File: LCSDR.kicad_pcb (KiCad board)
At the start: 2 copper layers, 150 x 95 mm, 75 parts, among them J1 MIC_PTT, J10 Conn_01x01, J11 Conn_01x01, J13 Jack-DC, J2 Conn_01x30, J3 Audio-Jack-3_2Switches, J4 Conn_01x30, J5 USB_B_Mini, J6 IDC10 Serial Wire, J8 Conn_01x01, J9 Conn_01x01, U1 SI5351A, U16 WM8731_alt, U2 FM24CL16B, U3 STM32F401RCTx, U5 MC34063, U7 78M09, Y1 20Mhz, Y2 Crystal

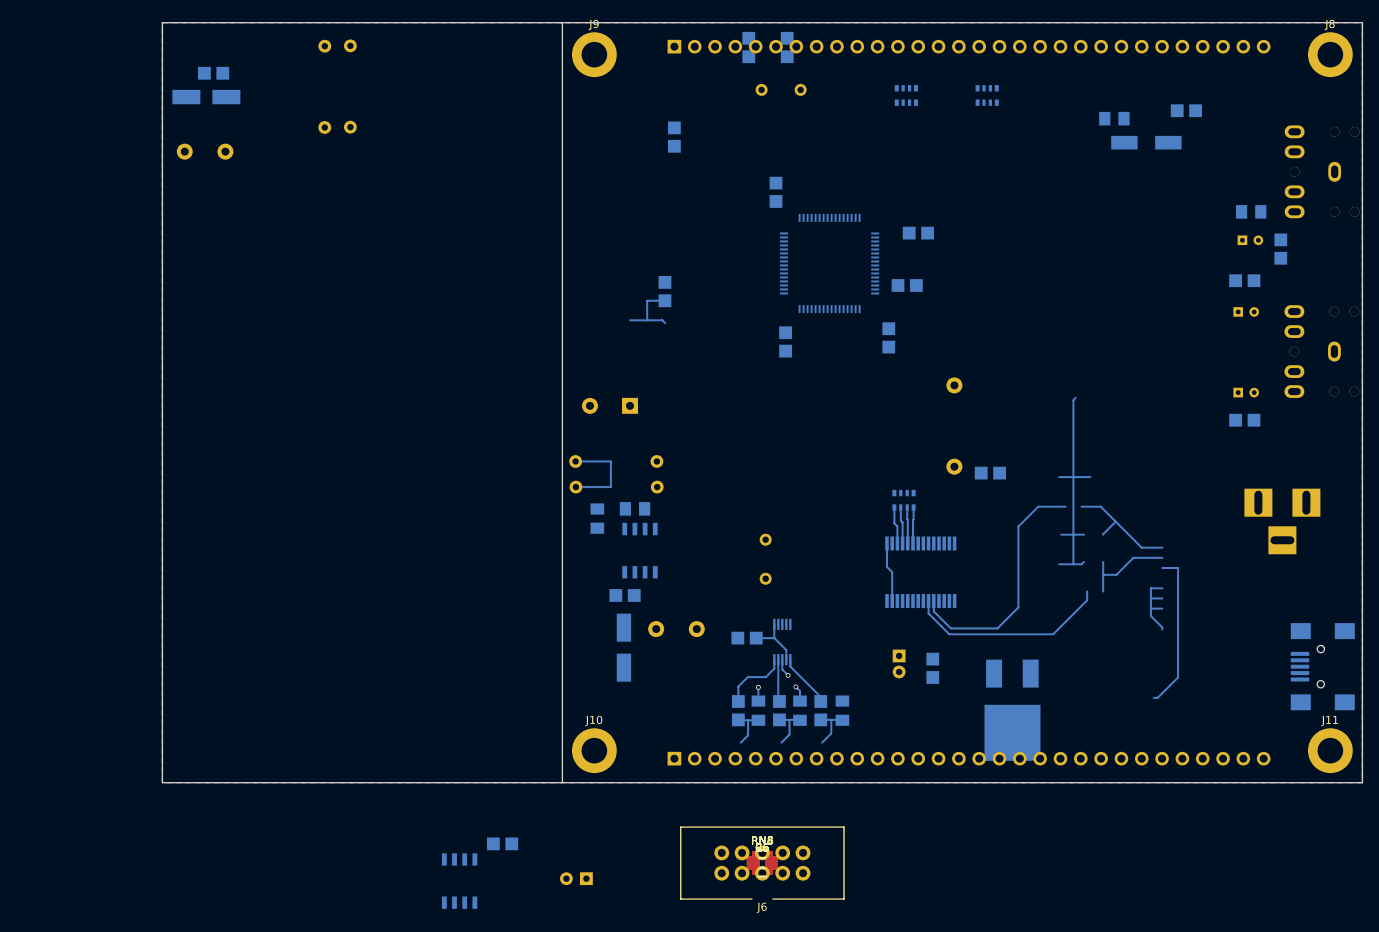
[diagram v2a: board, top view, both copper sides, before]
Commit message: PCB almost ready, needs some GND vias
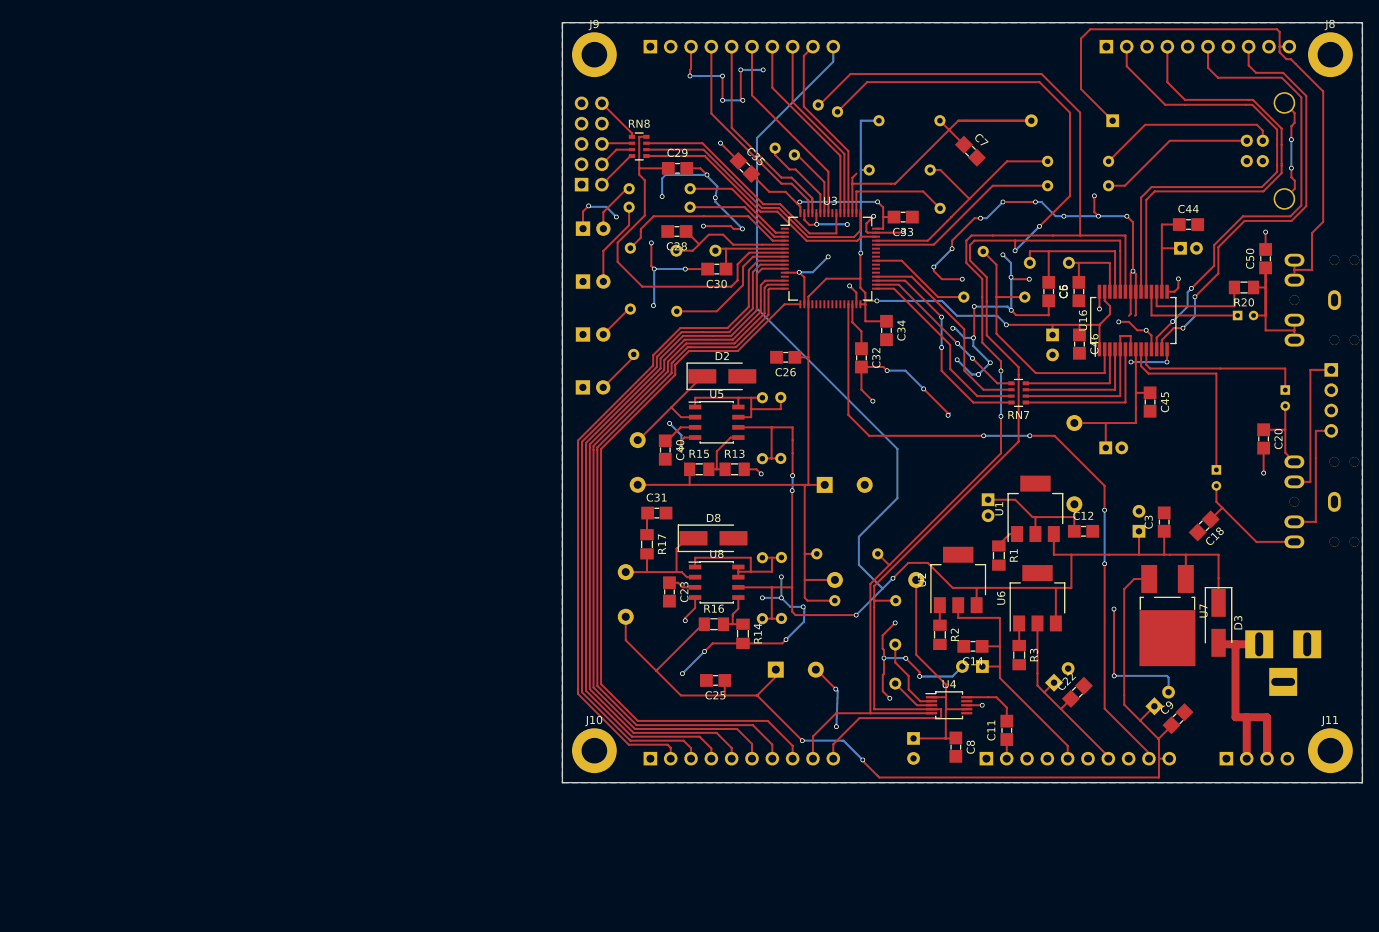
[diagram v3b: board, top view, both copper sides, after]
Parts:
- removed C2: 100nF, UI:C_1206_0603
- removed C36: 10uF, Capacitors_THT:CP_Radial_D6.3mm_P2.50mm
- removed C41: 180pF, UI:C_1206_0603
- removed RN2, RN3, RN4, RN5, RN6: 47, Resistors_SMD:R_Array_Convex_4x0603
- removed Y2: Crystal, Crystals:Crystal_HC49-U_Vertical
- added C10: 100uF, Capacitors_THT:CP_Radial_D6.3mm_P2.50mm, B.Cu at (167.5, 120.5)
- added C11: 100nF, UI:C_1206_0603, F.Cu at (170.6, 128.5)
- added C12: 100nF, UI:C_1206_0603, F.Cu at (180.1, 103.6)
- added C13: 100uF, Capacitors_THT:CP_Radial_D6.3mm_P2.50mm, B.Cu at (189.0, 125.5)
- added C14: 100nF, UI:C_1206_0603, F.Cu at (166.3, 118.0)
- added C15: 100uF, Capacitors_THT:CP_Radial_D6.3mm_P2.50mm, B.Cu at (158.9, 129.5)
- added C16: 100uF, Capacitors_THT:CP_Radial_D6.3mm_P2.50mm, B.Cu at (176.4, 122.5)
- added C21: 100uF, Capacitors_THT:CP_Radial_D6.3mm_P2.50mm, B.Cu at (187.1, 103.6)
- added C22: 100nF, UI:C_1206_0603, F.Cu at (179.4, 123.7)
- added C23: 180pF, UI:C_1206_0603, F.Cu at (128.4, 111.2)
- added C24: 1000uF, Capacitors_THT:CP_Radial_D10.0mm_P5.00mm, B.Cu at (141.7, 120.9)
- added C25: 100nF, UI:C_1206_0603, F.Cu at (134.2, 122.2)
- added C31: 100nF, UI:C_1206_0603, F.Cu at (126.8, 101.3)
- added C8: 100nF, UI:C_1206_0603, F.Cu at (164.2, 130.6)
- added C9: 100nF, UI:C_1206_0603, F.Cu at (191.9, 127.0)
- added D4: LED, LEDs:LED_D5.0mm_FlatTop, B.Cu at (117.6, 65.8)
- added D5: LED, LEDs:LED_D5.0mm_FlatTop, B.Cu at (117.6, 72.4)
- added D6: LED, LEDs:LED_D5.0mm_FlatTop, B.Cu at (117.6, 79.0)
- added D7: LED, LEDs:LED_D5.0mm_FlatTop, B.Cu at (117.6, 85.6)
- added D8: SS14, Diodes_SMD:D_SMA_Handsoldering, F.Cu at (133.9, 104.5)
- added J12: Conn_01x10, Pin_Headers:Pin_Header_Straight_1x10_Pitch2.54mm, B.Cu at (126.0, 43.0)
- added J14: Conn_01x04, Pin_Headers:Pin_Header_Straight_1x04_Pitch2.54mm, B.Cu at (198.0, 132.0)
- added J15: SPEAKER, Pin_Headers:Pin_Header_Straight_1x04_Pitch2.54mm, B.Cu at (211.1, 83.4)
- added J7: Conn_01x10, Pin_Headers:Pin_Header_Straight_1x10_Pitch2.54mm, B.Cu at (126.0, 132.0)
- added L1: 100uH, Choke_Axial_ThroughHole:Choke_Horizontal_RM10mm, B.Cu at (154.1, 109.7)
- added R14: 11k, UI:R_1206_0603, F.Cu at (137.6, 116.4)
- added R16: 18k, UI:R_1206_0603, F.Cu at (133.9, 115.2)
- added R17: 18k, UI:R_1206_0603, F.Cu at (125.6, 105.2)
- added R18: 4.7k, Resistors_THT:R_Axial_DIN0204_L3.6mm_D1.6mm_P7.62mm_Horizontal, B.Cu at (123.3, 60.8)
- added R19: 4.7k, Resistors_THT:R_Axial_DIN0204_L3.6mm_D1.6mm_P7.62mm_Horizontal, B.Cu at (123.3, 63.1)
- added R21: 4.7k, Resistors_THT:R_Axial_DIN0204_L3.6mm_D1.6mm_P7.62mm_Horizontal, B.Cu at (123.5, 75.8)
- added R22: 4.7k, Resistors_THT:R_Axial_DIN0204_L3.6mm_D1.6mm_P7.62mm_Horizontal, B.Cu at (123.9, 81.5)
- added R23: 47R, Resistors_THT:R_Axial_DIN0204_L3.6mm_D1.6mm_P7.62mm_Horizontal, B.Cu at (141.6, 55.7)
- added R24: 47R, Resistors_THT:R_Axial_DIN0204_L3.6mm_D1.6mm_P7.62mm_Horizontal, B.Cu at (183.3, 57.3)
- added R25: 47R, Resistors_THT:R_Axial_DIN0204_L3.6mm_D1.6mm_P7.62mm_Horizontal, B.Cu at (183.3, 60.4)
- added R26: 4.7k, Resistors_THT:R_Axial_DIN0204_L3.6mm_D1.6mm_P7.62mm_Horizontal, B.Cu at (153.3, 58.4)
- added R27: 47R, Resistors_THT:R_Axial_DIN0204_L3.6mm_D1.6mm_P7.62mm_Horizontal, B.Cu at (144.0, 56.5)
- added R7: 56, Resistors_THT:R_Axial_DIN0204_L3.6mm_D1.6mm_P7.62mm_Horizontal, B.Cu at (172.8, 74.3)
- added R8: 56, Resistors_THT:R_Axial_DIN0204_L3.6mm_D1.6mm_P7.62mm_Horizontal, B.Cu at (167.6, 68.6)
- added U4: SI5351A, Housings_SSOP:MSOP-10_3x3mm_Pitch0.5mm, F.Cu at (163.3, 125.3)
- added U6: LD1117S33TR, TO_SOT_Packages_SMD:SOT-223, F.Cu at (174.4, 111.9)
- added U8: MC34063, UI:SOIC-8_3.9x4.9mm_Pitch1.27mm, F.Cu at (134.3, 110.0)
- added Y3: 12.288Mhz, Crystals:Crystal_HC49-U_Vertical, B.Cu at (178.3, 70.0)
- added Y4: Crystal, Crystals:Crystal_HC49-U_Vertical, B.Cu at (156.6, 122.6)
- C1, C4: value 100nF -> 10uF; footprint UI:C_1206_0603 -> Capacitors_THT:CP_Radial_D5.0mm_P2.00mm
- C116: footprint Capacitors_ThroughHole:CP_Radial_D5.0mm_P2.00mm -> Capacitors_THT:CP_Radial_D5.0mm_P2.00mm
- C18, C20, C26, C28, C29, C3, C30, C32, C33, C34, C35, C40, C44, C45, C46, C50, C7, D2, D3, R13, R15, R20, RN7, U16, U3, U5, U7: moved to F.Cu
- C27: value 100nF -> 100uF; footprint UI:C_1206_0603 -> Capacitors_THT:CP_Radial_D6.3mm_P2.50mm
- C38: footprint Capacitors_ThroughHole:CP_Radial_D10.0mm_P5.00mm -> Capacitors_THT:CP_Radial_D10.0mm_P5.00mm
- D1: footprint Diodes_SMD:D_MiniMELF_Handsoldering -> Diodes_THT:D_DO-35_SOD27_P10.16mm_Horizontal
- J2, J4: value Conn_01x30 -> Conn_01x10; footprint Pin_Headers:Pin_Header_Straight_1x30_Pitch2.54mm -> Pin_Headers:Pin_Header_Straight_1x10_Pitch2.54mm
- J5: value USB_B_Mini -> USB_B; footprint Connectors:USB_Mini-B -> Connectors:USB_B
- J6: value IDC10 Serial Wire -> SWO; footprint UI:USBBLASTER -> Pin_Headers:Pin_Header_Straight_2x05_Pitch2.54mm; moved to B.Cu
- L2, L3: footprint Choke_Toroid_ThroughHole:Choke_Toroid_5x10mm_Vertical -> Choke_Toroid_ThroughHole:Choke_Toroid_6,5x13mm_Vertical
- R1, R2, R3: value 100 -> 10; moved to F.Cu
- R10, R11, R12, R9: footprint Resistors_ThroughHole:R_Axial_DIN0207_L6.3mm_D2.5mm_P10.16mm_Horizontal -> Resistors_THT:R_Axial_DIN0204_L3.6mm_D1.6mm_P7.62mm_Horizontal
- R4: footprint UI:R_1206_0603 -> Resistors_THT:R_Axial_DIN0204_L3.6mm_D1.6mm_P7.62mm_Horizontal
- R5, R6: footprint UI:R_1206_0603 -> Resistors_THT:R_Axial_DIN0204_L3.6mm_D1.6mm_P7.62mm_Horizontal; moved to B.Cu
- U1: value SI5351A -> LD1117S33TR; footprint Housings_SSOP:MSOP-10_3x3mm_Pitch0.5mm -> TO_SOT_Packages_SMD:SOT-223; moved to F.Cu
- U2: value FM24CL16B -> LD1117S33TR; footprint Housings_SOIC:SOIC-8_3.9x4.9mm_Pitch1.27mm -> TO_SOT_Packages_SMD:SOT-223; moved to F.Cu
- moved D3 142.6 mm to (197.0, 115.0), turned to 270 degrees
- moved J2 104.1 mm to (183.0, 43.0)
- moved J4 97.2 mm to (168.0, 132.0)
- moved C27 93.7 mm to (176.3, 79.0), turned to 270 degrees
- moved RN8 90.9 mm to (124.6, 55.5)
- moved R10 88.2 mm to (140.0, 114.5), turned to 90 degrees
- moved J6 87.8 mm to (117.4, 60.2)
- moved C5 81.7 mm to (179.6, 73.6), turned to 90 degrees
- moved C6 79.9 mm to (175.8, 73.6), turned to 270 degrees
- moved R12 78.4 mm to (142.4, 106.8), turned to 270 degrees
- moved U2 72.8 mm to (164.5, 109.7)
- moved L3 67.5 mm to (116.3, 108.2), turned to 0 degrees
- moved C44 64.0 mm to (193.3, 65.2), turned to 0 degrees
- moved J5 63.9 mm to (200.6, 57.3), turned to 0 degrees
- moved C116 61.9 mm to (192.3, 68.2), turned to 0 degrees
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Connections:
- net MIC_BIAS renamed Net-(R20-Pad2)
- net MIC_IN renamed Net-(C49-Pad1)
- C1 pad 1: +3V3 -> Net-(C1-Pad1)
- C3 pad 1: CLK1 -> +12V
- C3 pad 2: Net-(C3-Pad2) -> GND
- C4 pad 1: CLK0 -> ANALOG_PS_AC
- C4 pad 2: Net-(C4-Pad2) -> GND
- C45 pad 1: GND -> Net-(C1-Pad1)
- C45 pad 2: Net-(C45-Pad2) -> GND
- D1 pad 1: Net-(D1-Pad1) -> PTT
- D3 pad 1: Net-(D3-Pad1) -> +12V
- D3 pad 2: GND -> +12VA
- J1 pad 2: Net-(D1-Pad1) -> PTT
- J1 pad 5: Net-(D1-Pad1) -> PTT
- J13 pad 1: +12V -> +12VA
- J2 pad 10: Net-(J2-Pad10) -> PTT
- J2 pad 2: CLK2 -> LINE_IN_LEFT
- J2 pad 4: CLK1 -> LINE_IN_RIGHT
- J2 pad 6: CLK0 -> LINE_OUT_LEFT
- J2 pad 7: Net-(J2-Pad7) -> GND
- J2 pad 8: Net-(J2-Pad8) -> LINE_OUT_RIGHT
- J2 pad 9: Net-(J2-Pad9) -> GND
- J3 pad 1: Net-(C19-Pad2) -> Net-(C17-Pad2)
- J3 pad 2: Net-(C17-Pad2) -> Net-(C19-Pad2)
- J4 pad 1: Net-(J4-Pad1) -> GND
- J4 pad 10: GND -> +9V
- J4 pad 2: Net-(J4-Pad2) -> CLK
- J4 pad 3: Net-(J4-Pad3) -> GND
- J4 pad 4: Net-(J4-Pad4) -> GND
- J4 pad 5: Net-(J4-Pad5) -> ROTATOR
- J4 pad 6: Net-(J4-Pad6) -> GND
- J4 pad 7: Net-(J4-Pad7) -> MIXER
- J4 pad 8: Net-(J4-Pad8) -> GND
- J4 pad 9: ADC -> IF_RX_TX
- J5 pad 1: Net-(J5-Pad1) -> (no net)
- J5 pad 4: Net-(J5-Pad4) -> GND
- J6 pad 1: MCU_VOLTAGE_33V -> (no net)
- J6 pad 7: Net-(J6-Pad7) -> (no net)
- J6 pad 8: Net-(J6-Pad8) -> (no net)
- L3 pad 1: Net-(D3-Pad1) -> Net-(D8-Pad1)
- L4 pad 1: Net-(C45-Pad2) -> ANALOG_PS_AC
- L4 pad 2: +3V3 -> Net-(C1-Pad1)
- R1 pad 1: CLK2 -> Net-(R1-Pad1)
- R12 pad 2: Net-(R12-Pad2) -> +12V
- R2 pad 1: CLK1 -> Net-(R2-Pad1)
- R3 pad 1: CLK0 -> Net-(R3-Pad1)
- RN8 pad 1: Net-(J6-Pad2) -> Net-(J6-Pad10)
- RN8 pad 2: Net-(J6-Pad4) -> Net-(J6-Pad6)
- RN8 pad 3: Net-(J6-Pad6) -> Net-(J6-Pad4)
- RN8 pad 4: Net-(J6-Pad10) -> Net-(J6-Pad2)
- RN8 pad 5: MCU_RESET -> SWDIO
- RN8 pad 6: SWO -> SWCLK
- RN8 pad 7: SWCLK -> SWO
- RN8 pad 8: SWDIO -> MCU_RESET
- U1 pad 1: +3V3 -> Net-(R1-Pad1)
- U1 pad 2: Net-(U1-Pad2) -> ANALOG_PS_AC
- U1 pad 3: Net-(U1-Pad3) -> +12V
- U1 pad 4: I2C_SCL -> (no net)
- U16 pad 14: Net-(C45-Pad2) -> Net-(C1-Pad1)
- U16 pad 8: Net-(C45-Pad2) -> Net-(C1-Pad1)
- U2 pad 1: Net-(U2-Pad1) -> Net-(R2-Pad1)
- U2 pad 2: Net-(U2-Pad2) -> ROTATOR
- U2 pad 3: Net-(U2-Pad3) -> +12V
- U2 pad 4: GND -> (no net)
- U3 pad 1: Net-(U3-Pad1) -> (no net)
- U3 pad 10: BAND2 -> IO4
- U3 pad 11: BAND3 -> IO5
- U3 pad 13: Net-(U3-Pad13) -> (no net)
- U3 pad 14: ATT -> IO6
- U3 pad 15: PREAMP -> IO7
- U3 pad 16: Net-(U3-Pad16) -> IO8
- U3 pad 17: Net-(U3-Pad17) -> IO9
- U3 pad 2: KEY_B -> LED3
- U3 pad 20: Net-(U3-Pad20) -> (no net)
- U3 pad 21: TX1 -> (no net)
- U3 pad 22: ENCODER_A -> (no net)
- U3 pad 23: ENCODER_B -> (no net)
- U3 pad 24: ADC -> (no net)
- U3 pad 25: Net-(U3-Pad25) -> (no net)
- U3 pad 26: Net-(U3-Pad26) -> (no net)
- U3 pad 27: Net-(U3-Pad27) -> (no net)
- U3 pad 28: Net-(U3-Pad28) -> (no net)
- U3 pad 29: Net-(U3-Pad29) -> IF_RX_TX
- U3 pad 3: KEY_C -> LED2
- U3 pad 37: I2S_MCLK -> (no net)
- U3 pad 38: Net-(U3-Pad38) -> (no net)
- U3 pad 39: TX2 -> (no net)
- U3 pad 4: KEY_D -> LED1
- U3 pad 40: I2C_SDA_MCU -> I2S_CLKIN_MCU
- U3 pad 41: I2C_SCL_MCU -> (no net)
- U3 pad 42: Net-(U3-Pad42) -> (no net)
- U3 pad 43: Net-(U3-Pad43) -> (no net)
- U3 pad 50: LCD_CE -> I2S_CLKIN_TEST_MCU
- U3 pad 51: LCD_CLK -> PTT_IN
- U3 pad 52: LCD_DC -> S2_RX_TX
- U3 pad 53: LCD_DIN -> S1_RX_TX
- U3 pad 54: Net-(U3-Pad54) -> IO3
- U3 pad 56: LCD_LIGHT -> (no net)
- U3 pad 57: I_IN_M2 -> IO2
- U3 pad 58: Q_IN_M1 -> I2C_SCL_MCU
- U3 pad 59: Q_IN_M2 -> I2C_SDA_MCU
- U3 pad 61: Net-(U3-Pad61) -> IO1
- U3 pad 62: Net-(U3-Pad62) -> IO0
- U3 pad 8: IO0 -> LED0
- U3 pad 9: BAND1 -> BAND
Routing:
- net GND: track 5.97 -> 329.4 mm, vias 3 -> 79
- net +12V: track 12.0 -> 219.4 mm, vias 0 -> 4
- net I2C_SCL: track 0.00 -> 175.8 mm, vias 0 -> 2
- net I2C_SDA: track 0.00 -> 167.5 mm, vias 0 -> 2
- net +3V3: track 24.0 -> 179.0 mm, vias 0 -> 5
- net +9V: track 0.00 -> 128.3 mm, vias 0 -> 2
- net IO9: track 0.00 -> 91.3 mm
- net IO8: track 0.00 -> 90.7 mm
- net IO7: track 0.00 -> 89.6 mm
- net IO5: track 0.00 -> 88.3 mm
- net IO6: track 0.00 -> 88.2 mm
- net (no net): track 87.2 -> 0.00 mm
- net IO4: track 0.00 -> 87.1 mm
- net BAND: track 0.00 -> 86.0 mm
- net IF_RX_TX: track 0.00 -> 86.0 mm, vias 0 -> 4
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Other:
- board size 150 x 95 mm -> 100 x 95 mm

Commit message: edit
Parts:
- moved R21 1.12 mm to (124.6, 76.0)
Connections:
- J7 pad 3: IO4 -> GND
- J7 pad 4: IO5 -> (no net)
- J7 pad 5: IO6 -> GND
- U3 pad 10: IO4 -> (no net)
- U3 pad 11: IO5 -> (no net)
- U3 pad 14: IO6 -> BAND
- U3 pad 9: BAND -> (no net)
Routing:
- net GND: track 329.4 -> 484.2 mm, vias 79 -> 113
- net IO5: track 88.3 -> 0.00 mm
- net IO6: track 88.2 -> 0.00 mm
- net IO4: track 87.1 -> 0.00 mm
- net BAND: track 86.0 -> 80.6 mm
- net Net-(D6-Pad2): track 4.71 -> 6.62 mm
- net MCU_RESET: track 47.0 -> 46.4 mm
- net LED1: track 22.9 -> 22.4 mm

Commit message: production
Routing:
- net GND: track 484.2 -> 898.3 mm, vias 113 -> 202

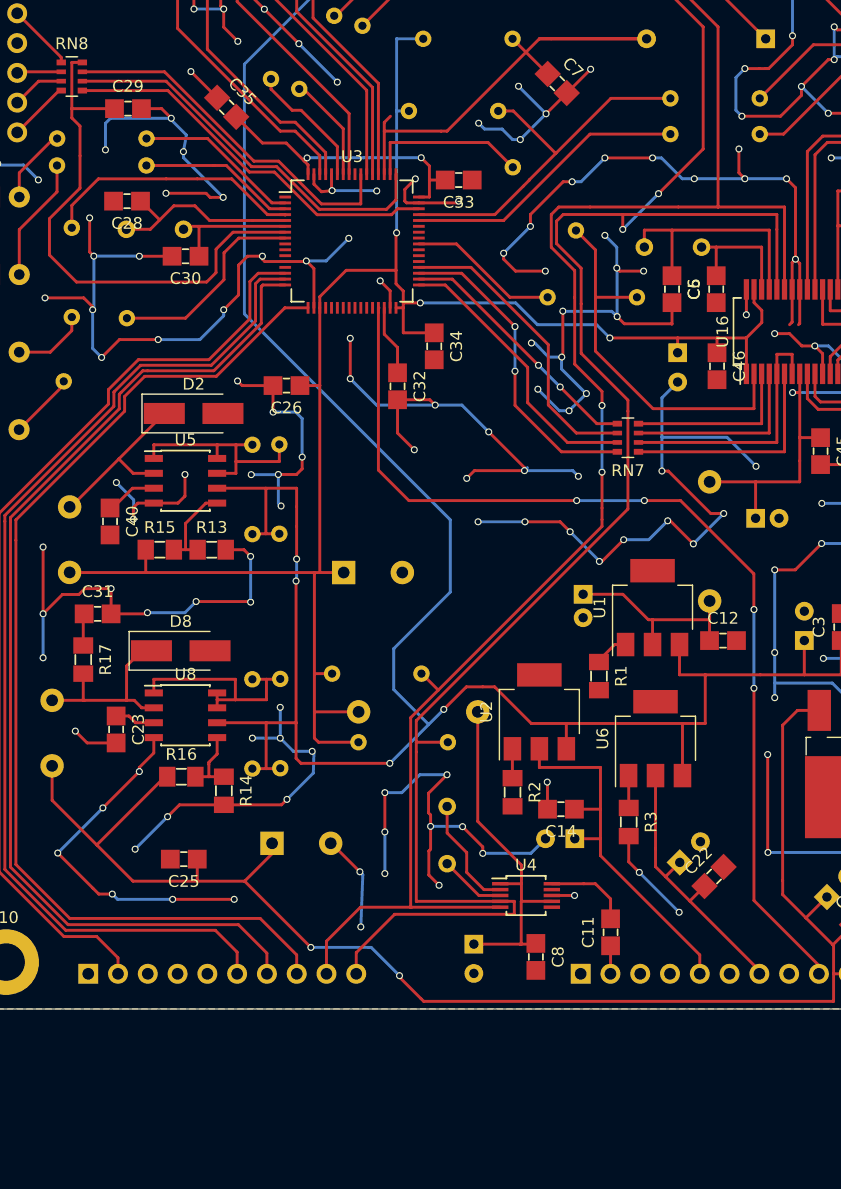
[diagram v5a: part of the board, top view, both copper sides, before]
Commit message: PCB for 98.304Mhz generator
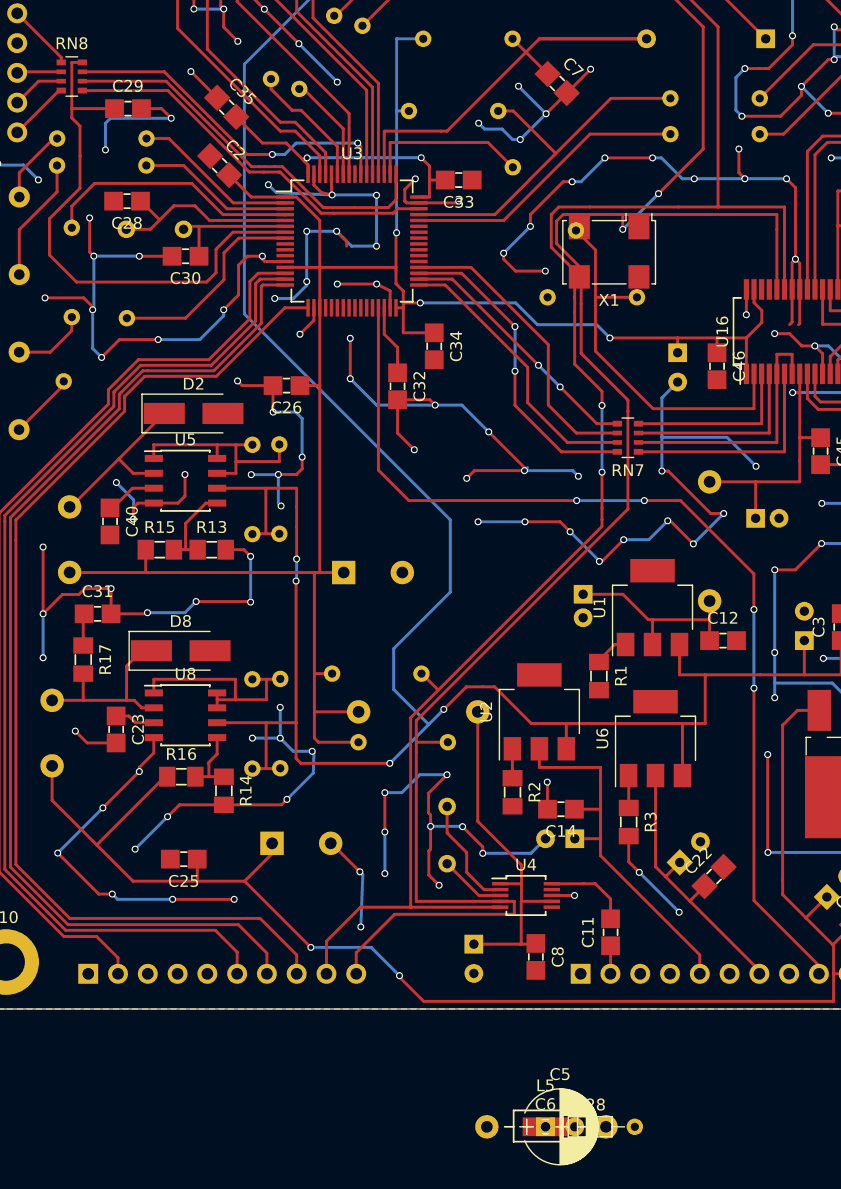
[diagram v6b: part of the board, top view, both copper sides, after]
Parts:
- removed Y3: 12.288Mhz, Crystals:Crystal_HC49-U_Vertical
- added C2: 100nF, UI:C_1206_0603, F.Cu at (137.2, 63.1)
- added L5: 100uH, Choke_Axial_ThroughHole:Choke_Horizontal_RM10mm, F.Cu at (165.0, 145.1)
- added R28: 56, Resistors_THT:R_Axial_DIN0204_L3.6mm_D1.6mm_P7.62mm_Horizontal, F.Cu at (165.0, 145.1)
- added X1: 98,304Mhz, Oscillators:Oscillator_SMD_IQD_IQXO70-4pin_7.5x5.0mm, F.Cu at (170.4, 70.5)
- C5: value 22pF -> 100uF; footprint UI:C_1206_0603 -> Capacitors_THT:CP_Radial_D6.3mm_P2.50mm
- C6: value 22pF -> 100nF
- U3: footprint Housings_QFP:LQFP-64_10x10mm_Pitch0.5mm -> Housings_QFP:TQFP-64_10x10mm_Pitch0.5mm
- Y1: value 20Mhz -> 8Mhz
- moved C5 72.9 mm to (165.0, 145.1), turned to 0 degrees
- moved C6 72.3 mm to (165.0, 145.1), turned to 0 degrees
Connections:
- C5 pad 1: GND -> Net-(C5-Pad1)
- C5 pad 2: Net-(C5-Pad2) -> GND
- C6 pad 1: Net-(C6-Pad1) -> Net-(C5-Pad1)
- R7 pad 1: CLKOUT_WM8731 -> Net-(R7-Pad1)
- R7 pad 2: I2S_CLKIN_MCU -> I2S_CORE_FREQ
- R8 pad 1: CLKOUT_WM8731 -> Net-(R7-Pad1)
- U16 pad 2: CLKOUT_WM8731 -> (no net)
- U16 pad 25: Net-(C6-Pad1) -> Net-(R7-Pad1)
- U16 pad 26: Net-(C5-Pad2) -> (no net)
- U3 pad 1: (no net) -> +3V3
- U3 pad 13: (no net) -> +3V3
- U3 pad 37: (no net) -> I2S_CORE_FREQ
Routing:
- net Net-(R28-Pad1): track 0.00 -> 66.5 mm, vias 0 -> 2
- net I2C_SDA: track 167.5 -> 126.2 mm, vias 2 -> 0
- net Net-(R7-Pad1): track 0.00 -> 33.0 mm
- net CLKOUT_WM8731: track 33.0 -> 0.00 mm
- net GND: track 898.3 -> 868.8 mm, vias 202 -> 195
- net I2C_SCL: track 175.8 -> 150.6 mm
- net Net-(C6-Pad1): track 21.1 -> 0.00 mm
- net +3V3: track 179.0 -> 196.8 mm
- net I2S_CLKIN_MCU: track 12.9 -> 0.00 mm
- net Net-(C5-Pad2): track 11.2 -> 0.00 mm
- net PTT_IN: track 44.2 -> 42.7 mm
- net SWO: track 30.9 -> 29.6 mm, vias 0 -> 2
